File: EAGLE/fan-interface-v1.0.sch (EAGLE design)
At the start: 27 parts, among them J2 QWIIC_RIGHT_ANGLE, U1 SN74LVC2G14DBVT, U2 SN74LVC2G14DBVT

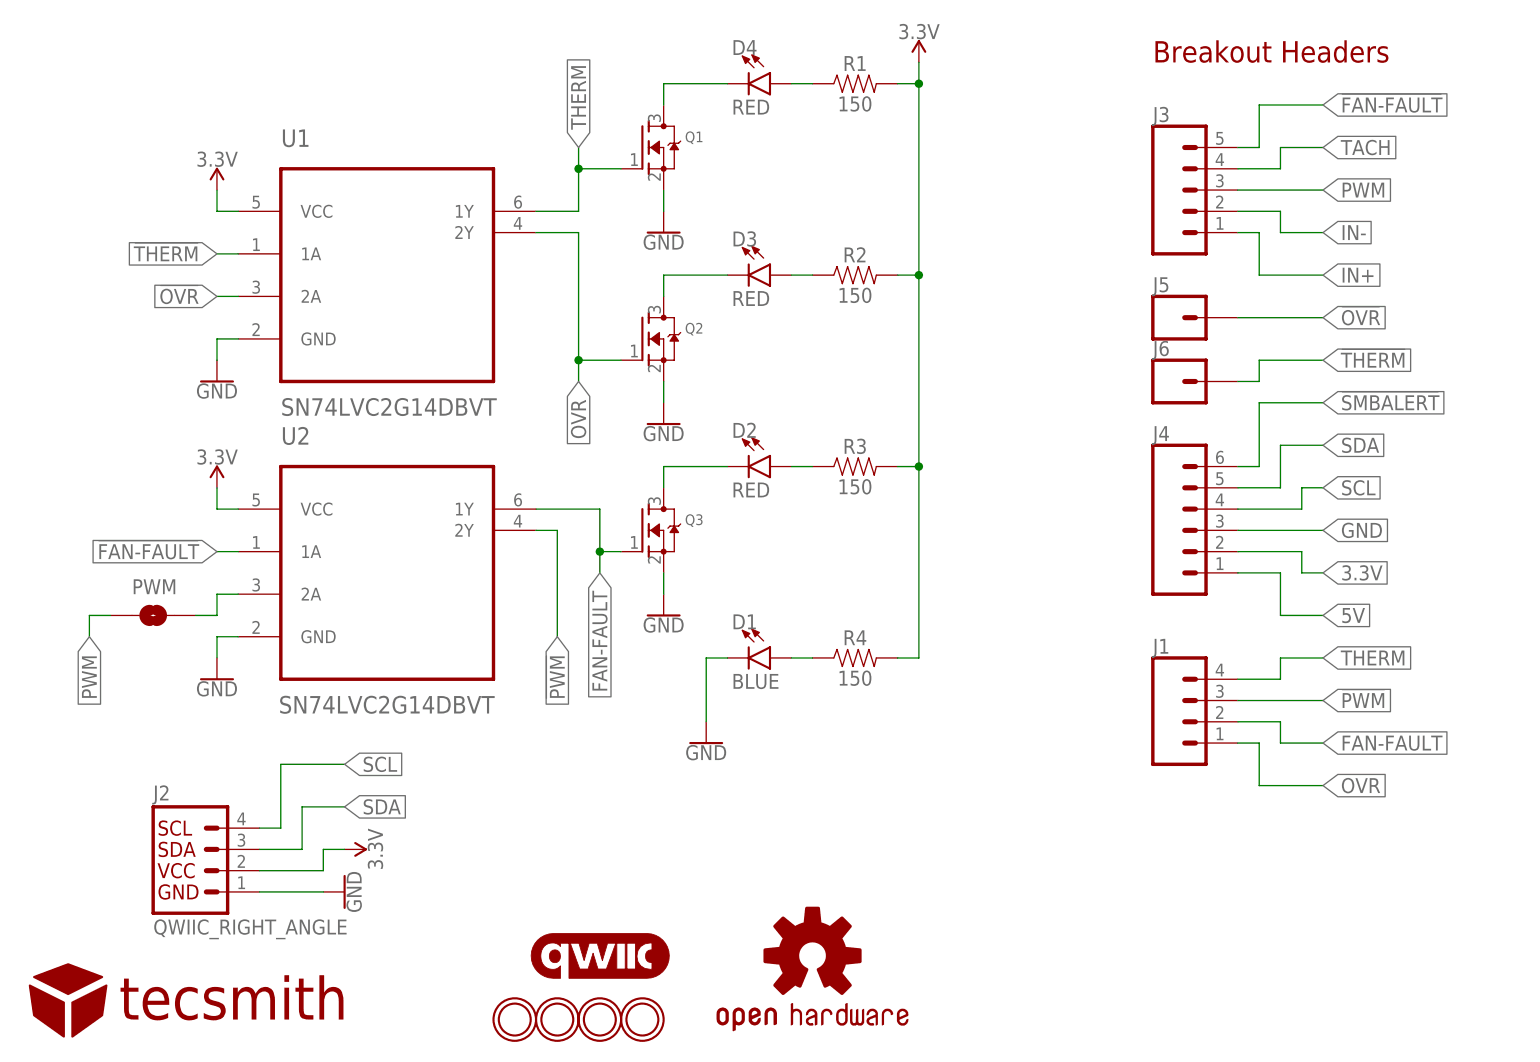
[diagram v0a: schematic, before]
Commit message: added active buzzer
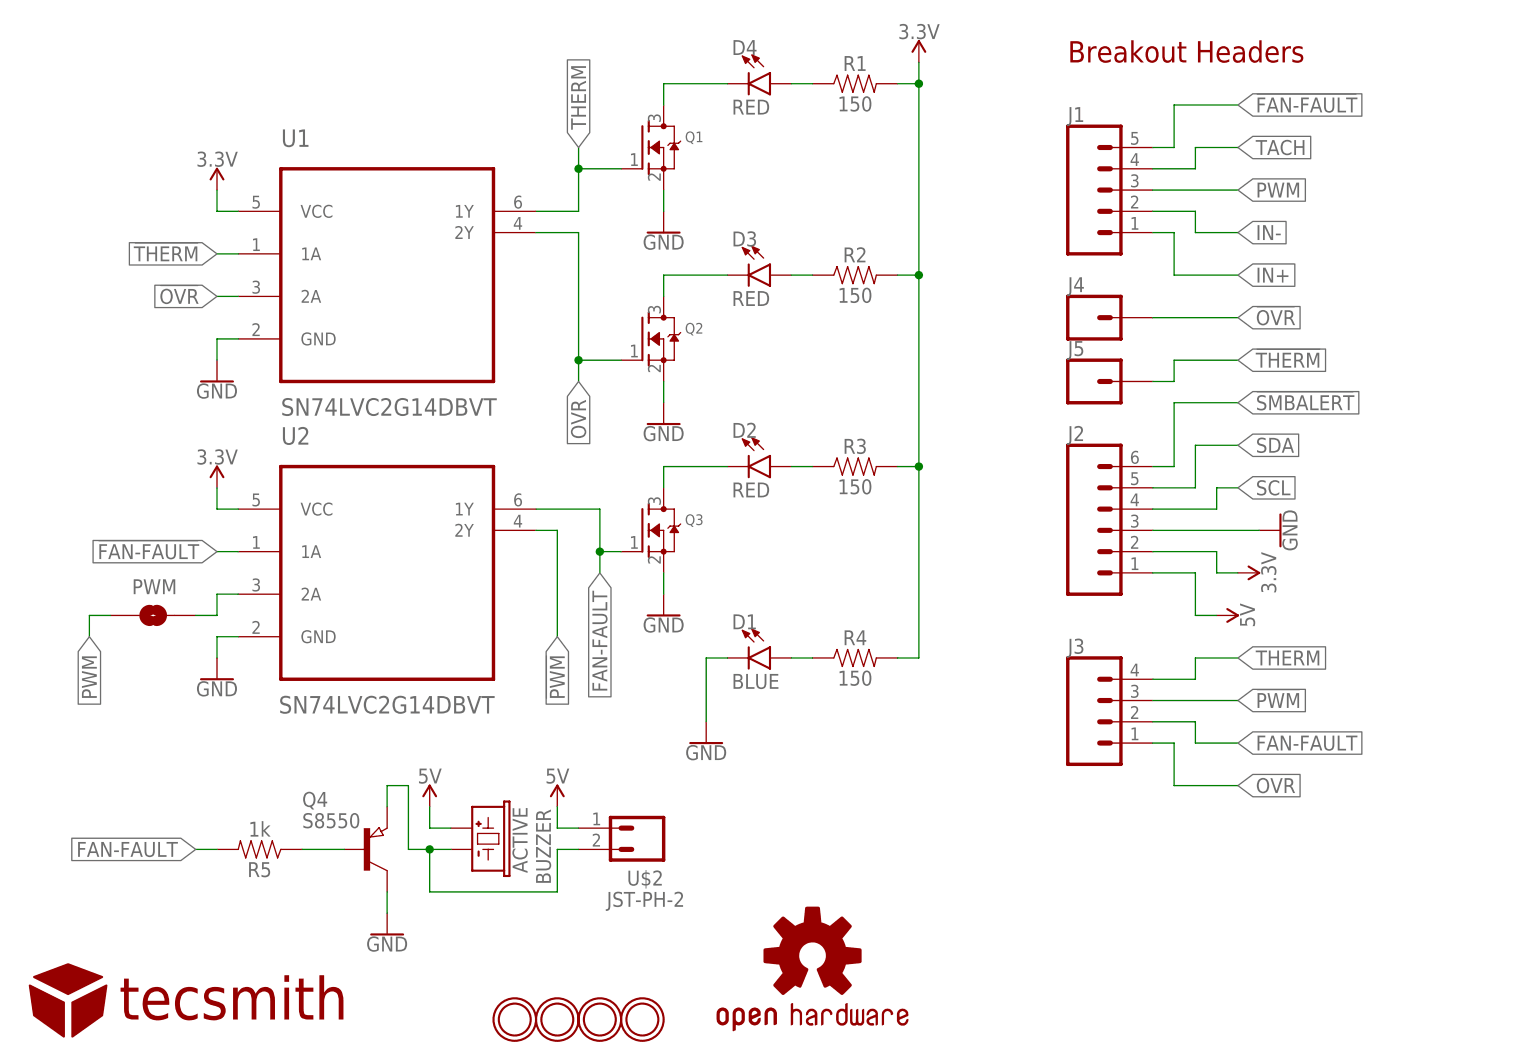
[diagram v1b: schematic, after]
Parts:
- removed J6: (no value), SparkFun-Connectors:CONN_01
- removed LOGO2: QWIIC_LOGO_3MM, SparkFun-Aesthetics:QWIIC_LOGO_3MM
- added ACTIVE: BUZZER, VinoRodrigues_Custom_Eagle:BUZZER
- added Q4: S8550, semicon-smd-ipc:PNP-TRANSISTOR_SOT23
- added R5: 1k, SparkFun-Resistors:1KOHM-0603-1/10W-1%
- added U$2: JST-PH-2, VinoRodrigues_Custom_Eagle:JST-PH-2
- J1: device SparkFun-Connectors:CONN_04PTH -> SparkFun-Connectors:CONN_05
- J2: value QWIIC_RIGHT_ANGLE -> (none); device SparkFun-Connectors:QWIIC_CONNECTORJS-1MM -> SparkFun-Connectors:CONN_06SILK_FEMALE_PTH
- J3: device SparkFun-Connectors:CONN_05 -> SparkFun-Connectors:CONN_04PTH
- J4: device SparkFun-Connectors:CONN_06SILK_FEMALE_PTH -> SparkFun-Connectors:CONN_01
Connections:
- new net N$11: ACTIVE.2, Q4.E, U$2.2
- new net N$7: Q4.B, R5.1
- net !FAN-FAULT: now also J1.5; no longer J3.5
- net !OVR: now also J4.1; no longer J5.1
- net !PWM: now also J3.3; no longer J1.3
- net !SMBALERT: now also J2.6; no longer J4.6
- net !THERM: now also J5.1; no longer J6.1
- net 3.3V: no longer J4.2
- net 5V: now also ACTIVE.1, J2.1, U$2.1; no longer J4.1
- net FAN-FAULT: now also J3.2, R5.2; no longer J1.2
- net GND: now also J2.3, Q4.C; no longer J2.1, J4.3
- net IN+: now also J1.1; no longer J3.1
- net IN-: now also J1.2; no longer J3.2
- net OVR: now also J3.1; no longer J1.1
- net PWM: now also J1.3; no longer J3.3
- net SCL: no longer J4.4
- net SDA: now also J2.5; no longer J2.3, J4.5
- net TACH: now also J1.4; no longer J3.4
- net THERM: now also J3.4; no longer J1.4
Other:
- moved on the sheet: J5
